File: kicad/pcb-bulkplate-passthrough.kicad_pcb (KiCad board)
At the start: 2 copper layers, 60.8 x 64.2 mm, 9 parts, among them J1 2601-3108

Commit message: done
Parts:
- removed REF** (x2): PinSocket_1x04_P1.27mm_Vertical, Connector_PinSocket_1.27mm:PinSocket_1x04_P1.27mm_Vertical
- removed REF** (x4): PinSocket_1x04_P2.54mm_Vertical, Connector_PinSocket_2.54mm:PinSocket_1x04_P2.54mm_Vertical
- removed REF** (x2): PinHeader_1x04_P1.27mm_Vertical, Connector_PinHeader_1.27mm:PinHeader_1x04_P1.27mm_Vertical
- added H1: M3 Hole, MountingHole:MountingHole_3.2mm_M3, F.Cu at (77.0, 59.9)
- added J2: 2.54mm Header, Connector_PinSocket_2.54mm:PinSocket_1x02_P2.54mm_Vertical, B.Cu at (79.1, 67.0)
- added J3: 2.54mm Header, Connector_PinSocket_2.54mm:PinSocket_1x02_P2.54mm_Vertical, B.Cu at (75.5, 67.0)
- J1: value 2601-3108 -> 2601-3104; footprint 2601-3108:2601-3108 -> 2601-3104:CONN4_2601-3104_WAG
- moved J1 2.82 mm to (84.6, 61.6)
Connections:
- J1 pad 1: unconnected-(J1-Pin_1-Pad1) -> Net-(J1-Pin_1)
- J1 pad 2: unconnected-(J1-Pin_2-Pad2) -> Net-(J1-Pin_2)
- J1 pad 3: unconnected-(J1-Pin_3-Pad3) -> Net-(J1-Pin_3)
- J1 pad 4: unconnected-(J1-Pin_4-Pad4) -> Net-(J1-Pin_4)
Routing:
- net Net-(J1-Pin_2): track 0.00 -> 29.9 mm
- net Net-(J1-Pin_4): track 0.00 -> 27.7 mm
- net Net-(J1-Pin_3): track 0.00 -> 25.8 mm
- net Net-(J1-Pin_1): track 0.00 -> 18.2 mm
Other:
- board size 60.8 x 64.2 mm -> 25 x 16 mm
- board text removed: "1.27mm"
- board text removed: "2.54mm"

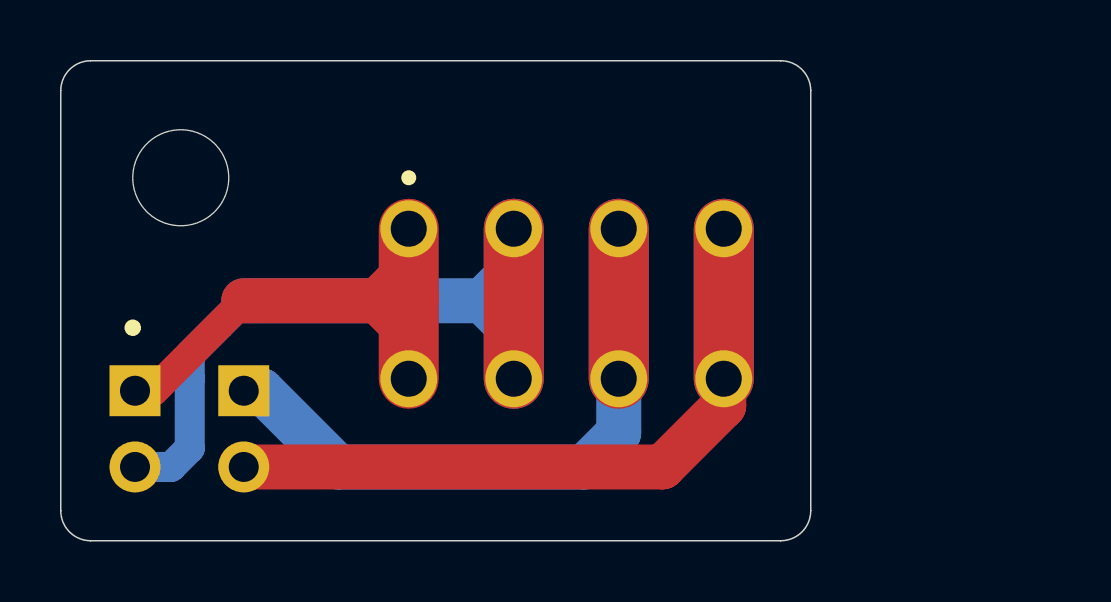
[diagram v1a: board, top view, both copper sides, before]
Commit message: added 2 hole variant
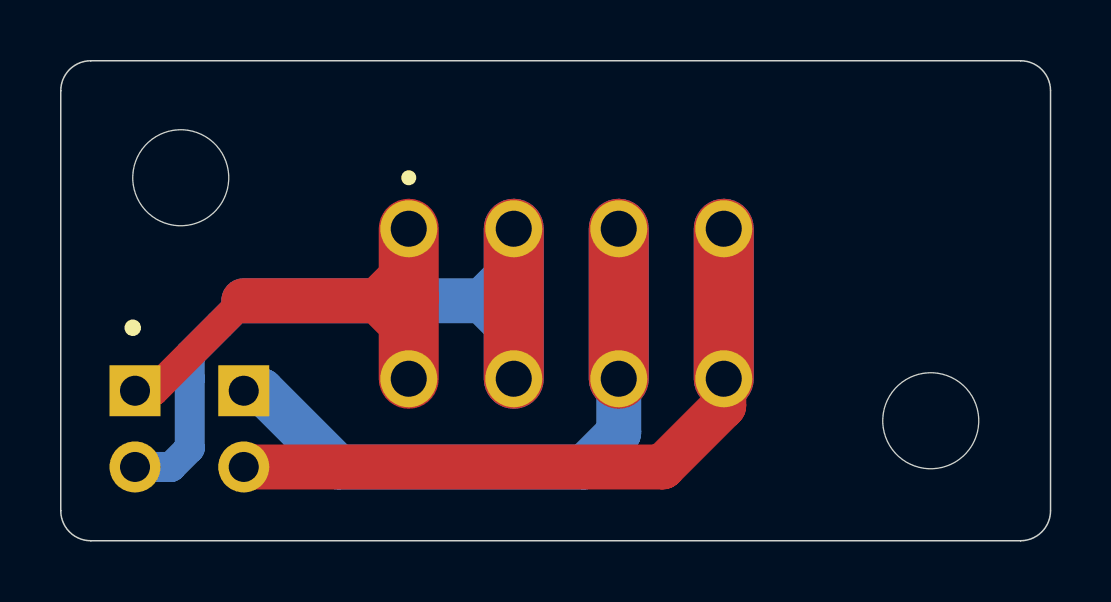
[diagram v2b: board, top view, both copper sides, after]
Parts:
- added H2: M3 Hole, MountingHole:MountingHole_3.2mm_M3, F.Cu at (102.0, 68.0)
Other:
- board size 25 x 16 mm -> 33 x 16 mm
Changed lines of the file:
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@@
+	(footprint "MountingHole:MountingHole_3.2mm_M3"
+		(layer "F.Cu")
+		(at 102 68)
+		(descr "Mounting Hole 3.2mm, M3, no annular, generated by kicad-footprint-generator mountinghole.py")
+		(tags "mountinghole M3")
+		(property "Reference" "H2"
+			(at 0 -4.15 0)
+			(layer "F.SilkS")
+			(hide yes)
+			(effects
+				(font
+					(size 1 1)
+					(thickness 0.15)
+				)
+			)
+		)
+		(property "Value" "M3 Hole"
+			(at 0 4.15 0)
+			(layer "F.Fab")
+			(hide yes)
+			(effects
+				(font
+					(size 1 1)
+					(thickness 0.15)
+				)
+			)
+		)
+		(property "Datasheet" ""
+			(at 0 0 0)
+			(layer "F.Fab")
+			(hide yes)
+			(effects
+				(font
+					(size 1.27 1.27)
+					(thickness 0.15)
+				)
+			)
+		)
+		(property "Description" "Mounting Hole without connection"
+			(at 0 0 0)
+			(layer "F.Fab")
+			(hide yes)
+			(effects
+				(font
+					(size 1.27 1.27)
+					(thickness 0.15)
+				)
+			)
+		)
+		(property ki_fp_filters "MountingHole*")
+		(sheetname "/")
+		(sheetfile "pcb-bulkplate-passthrough.kicad_sch")
+		(attr exclude_from_pos_files exclude_from_bom)
+		(fp_circle
+			(center 0 0)
+			(end 3.2 0)
+			(stroke
+				(width 0.15)
+				(type solid)
+			)
+			(fill no)
+			(layer "Cmts.User")
+		)
+		(fp_circle
+			(center 0 0)
+			(end 3.45 0)
+			(stroke
+				(width 0.05)
+				(type solid)
+			)
+			(fill no)
+			(layer "F.CrtYd")
+		)
+		(fp_text user "${REFERENCE}"
+			(at 0 0 0)
+			(layer "F.Fab")
+			(effects
+				(font
+					(size 1 1)
+					(thickness 0.15)
+				)
+			)
+		)
+		(pad "" np_thru_hole circle
+			(at 0 0)
+			(size 3.2 3.2)
+			(drill 3.2)
+			(layers "*.Cu" "*.Mask")
+		)
+		(embedded_fonts no)
+	)
 	(footprint "MountingHole:MountingHole_3.2mm_M3"
 		(layer "F.Cu")
@@
 	)
 	(gr_line
-		(start 97 56)
+		(start 77 59.9)
+		(end 102 59.9)
+		(stroke
+			(width 0.15)
+			(type default)
+		)
+		(layer "Dwgs.User")
+	)
+	(gr_line
+		(start 104.9929 56)
 		(end 74 56)
 		(stroke
@@
 	)
 	(gr_arc
-		(start 98 71)
-		(mid 97.707107 71.707107)
-		(end 97 72)
+		(start 105.992893 71)
+		(mid 105.7 71.707107)
+		(end 104.992893 72)
 		(stroke
 			(width 0.05)
@@
 	)
 	(gr_line
-		(start 98 57)
-		(end 98 71)
+		(start 105.992893 57)
+		(end 105.992893 71)
 		(stroke
 			(width 0.05)
@@
 	)
 	(gr_arc
-		(start 97 56)
-		(mid 97.707107 56.292893)
-		(end 98 57)
+		(start 104.992893 56)
+		(mid 105.7 56.292893)
+		(end 105.992893 57)
 		(stroke
 			(width 0.05)
@@
 	)
 	(gr_line
-		(start 97 72)
+		(start 104.992893 72)
 		(end 74 72)
 		(stroke
@@
 		(layer "Edge.Cuts")
 	)
+	(dimension
+		(type orthogonal)
+		(layer "Dwgs.User")
+		(pts
+			(xy 105.992893 71) (xy 73 71)
+		)
+		(height 7.3)
+		(orientation 0)
+		(format
+			(prefix "")
+			(suffix "")
+			(units 3)
+			(units_format 0)
+			(precision 4)
+			(suppress_zeroes yes)
+		)
+		(style
+			(thickness 0.15)
+			(arrow_length 1.27)
+			(text_position_mode 0)
+			(arrow_direction outward)
+			(extension_height 0.58642)
+			(extension_offset 0.5)
+			(keep_text_aligned yes)
+		)
+		(gr_text "32.9929"
+			(at 89.496446 77.15 0)
+			(layer "Dwgs.User")
+			(effects
+				(font
+					(size 1 1)
+					(thickness 0.15)
+				)
+			)
+		)
+	)
+	(dimension
+		(type orthogonal)
+		(layer "Dwgs.User")
+		(pts
+			(xy 85.1 72) (xy 85.5 56)
+		)
+		(height -19.8)
+		(orientation 1)
+		(format
+			(prefix "")
+			(suffix "")
+			(units 3)
+			(units_format 0)
+			(precision 4)
+			(suppress_zeroes yes)
+		)
+		(style
+			(thickness 0.15)
+			(arrow_length 1.27)
+			(text_position_mode 0)
+			(arrow_direction outward)
+			(extension_height 0.58642)
+			(extension_offset 0.5)
+			(keep_text_aligned yes)
+		)
+		(gr_text "16"
+			(at 64.15 64 90)
+			(layer "Dwgs.User")
+			(effects
+				(font
+					(size 1 1)
+					(thickness 0.15)
+				)
+			)
+		)
+	)
 	(segment
